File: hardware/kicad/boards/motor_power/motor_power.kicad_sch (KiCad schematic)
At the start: 65 parts, among them J1 PWM fra MCU, J2 MCP PWM, J3 DC Motor, J4 3-fase ind, J5 3-fase ud, J6 V1 ud til load, Q1 IRF540N, Q2 IRF530, SW1 Switch, U1 MCP601, U10 IL300, U11 MCP601, U2 NE555, U3 ILD74, U4 MCP601, U5 IR2110, U6 LM7805, U7 4N25, U8 IR2110, U9 MCP601

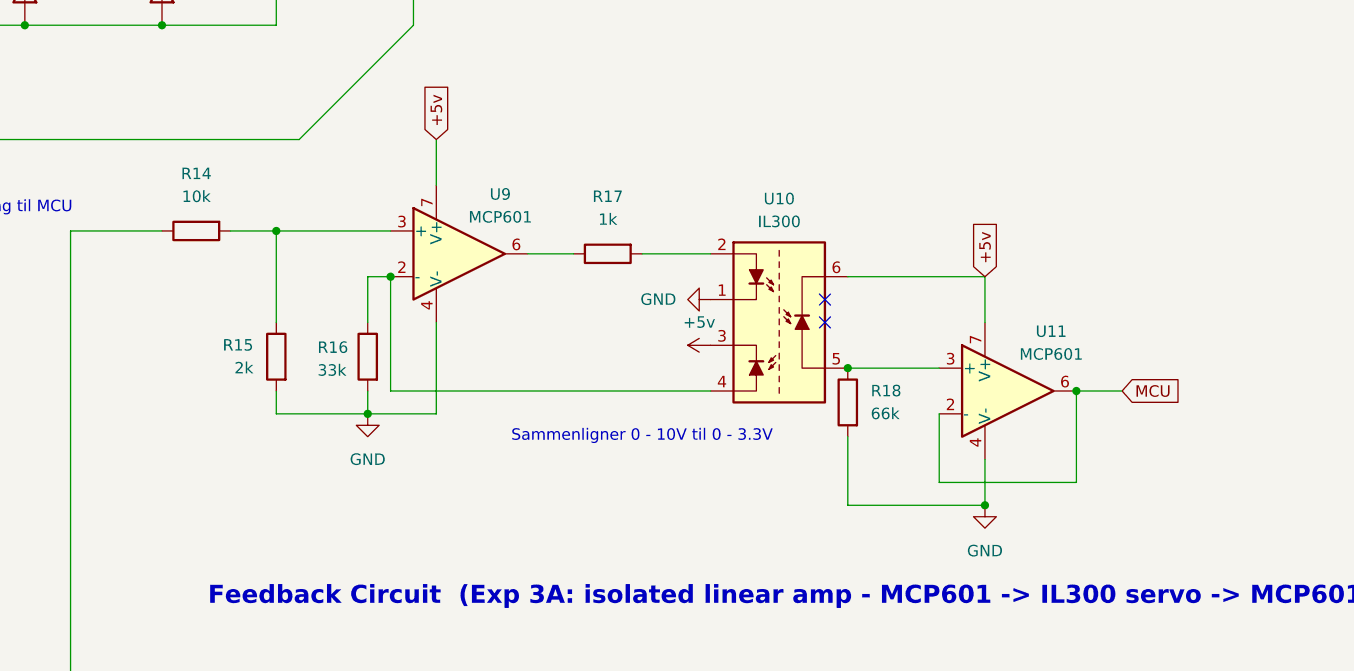
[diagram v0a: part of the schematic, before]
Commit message: motor_power: remove feedback amp and its leftover wiring (ERC 0, 57 parts)
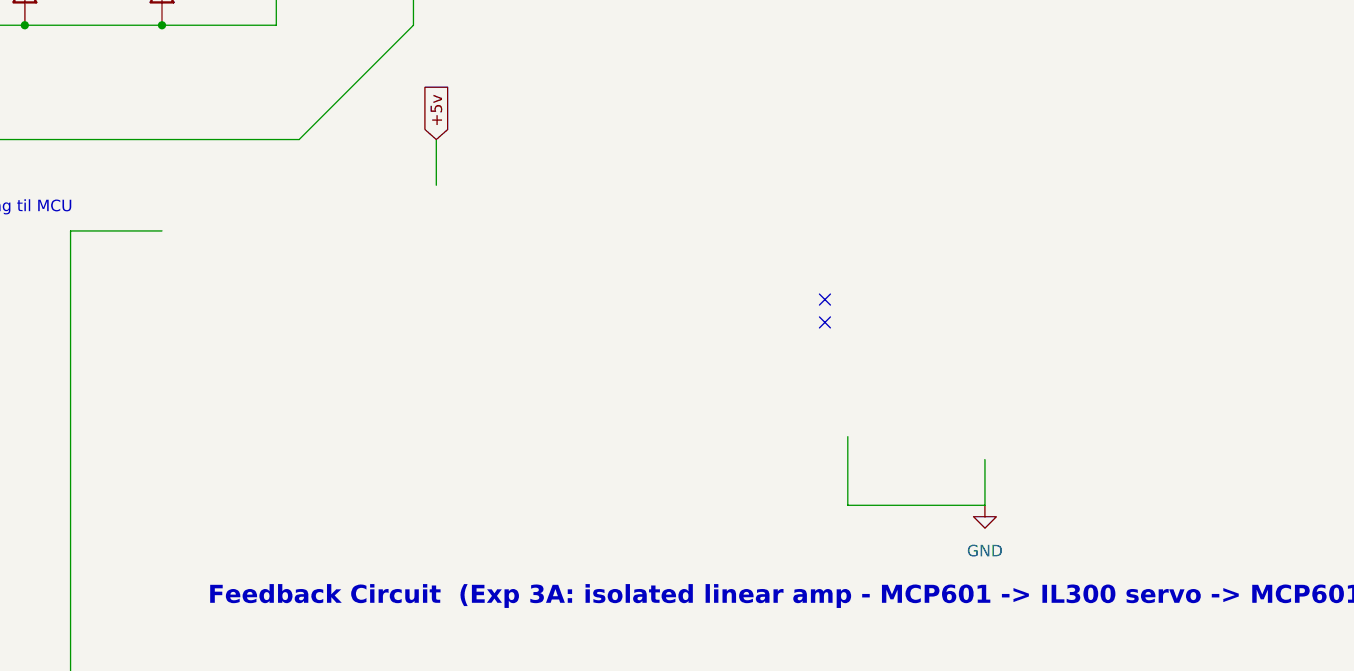
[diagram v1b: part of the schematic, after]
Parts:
- removed R14: 10k, Resistor_THT:R_Axial_DIN0207_L6.3mm_D2.5mm_P7.62mm_Horizontal, symbol Device:R
- removed R15: 2k, Resistor_THT:R_Axial_DIN0207_L6.3mm_D2.5mm_P7.62mm_Horizontal, symbol Device:R
- removed R16: 33k, Resistor_THT:R_Axial_DIN0207_L6.3mm_D2.5mm_P7.62mm_Horizontal, symbol Device:R
- removed R17: 1k, Resistor_THT:R_Axial_DIN0207_L6.3mm_D2.5mm_P7.62mm_Horizontal, symbol Device:R
- removed R18: 66k, Resistor_THT:R_Axial_DIN0207_L6.3mm_D2.5mm_P7.62mm_Horizontal, symbol Device:R
- removed U10: IL300, Package_DIP:DIP-8_W7.62mm_LongPads, symbol Isolator_Analog:IL300
- removed U11, U9: MCP601, Package_DIP:DIP-8_W7.62mm_LongPads, symbol Amplifier_Operational:MCP601-xP
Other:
- note removed: "Sammenligner 0 - 10V til 0 - 3.3V"

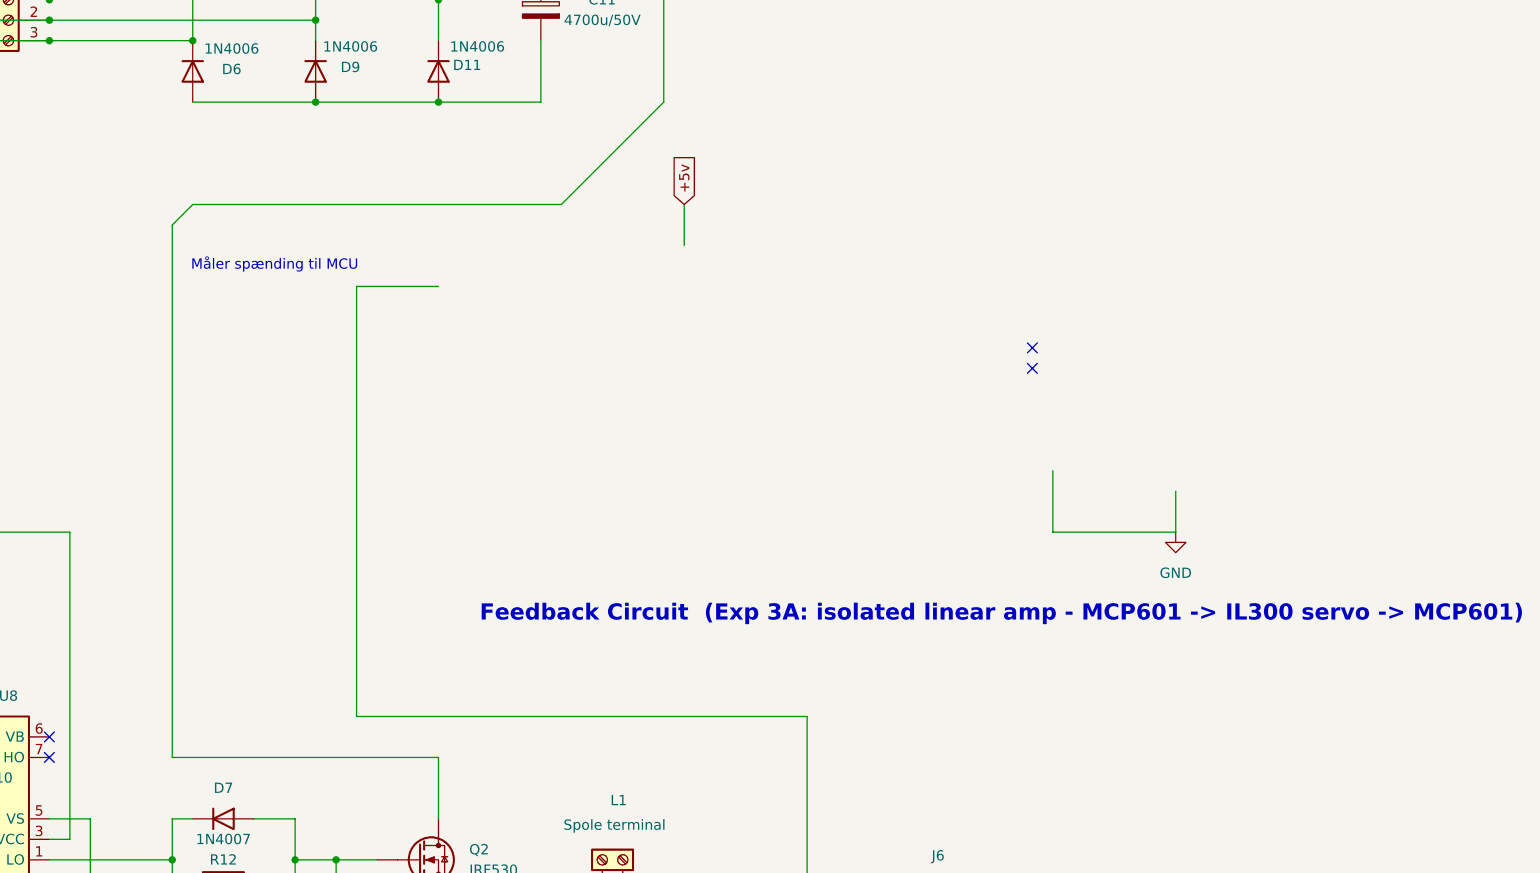
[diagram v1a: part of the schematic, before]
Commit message: motor_power: add J7 V1/GND/+5v sense connector to the feedback board
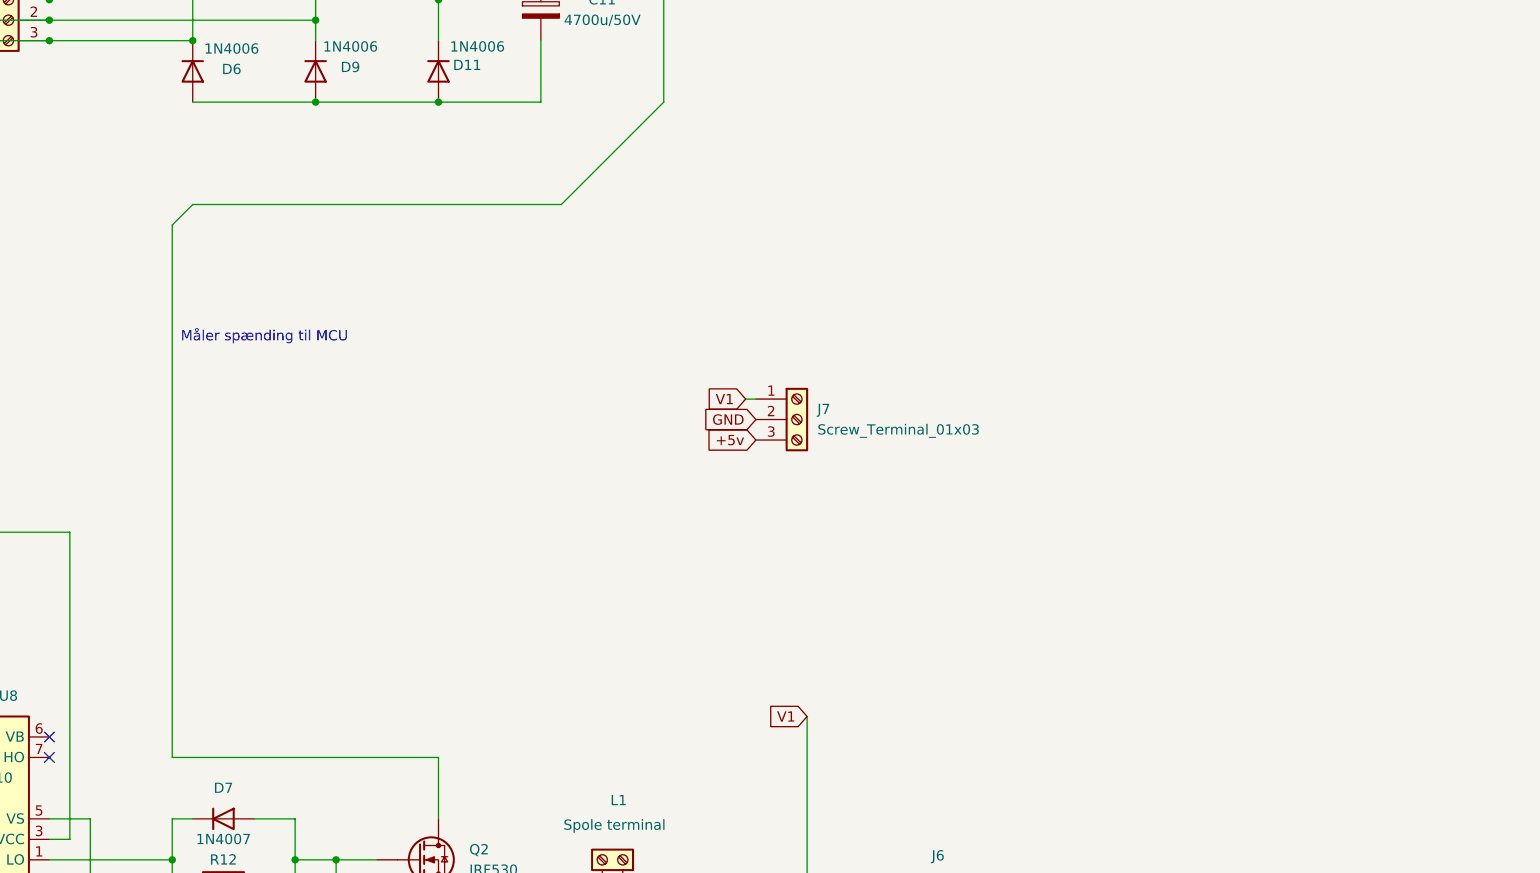
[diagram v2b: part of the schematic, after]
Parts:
- added J7: Screw_Terminal_01x03, TerminalBlock:TerminalBlock_bornier-3_P5.08mm, symbol Connector:Screw_Terminal_01x03
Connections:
- net +5v: now also J7.3 (Pin_3)
- net GND: now also J7.2 (Pin_2)
- net V1: now reaches C12.2 (Pin_2), J6.2 (Pin_2), L1.1 (Pin_1)
- net V1: now also J7.1 (Pin_1)
- no-connect marks 7 -> 5
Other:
- note removed: "Feedback Circuit (Exp 3A: isolated linear amp - MCP601 -> IL300 servo -> MCP601)"

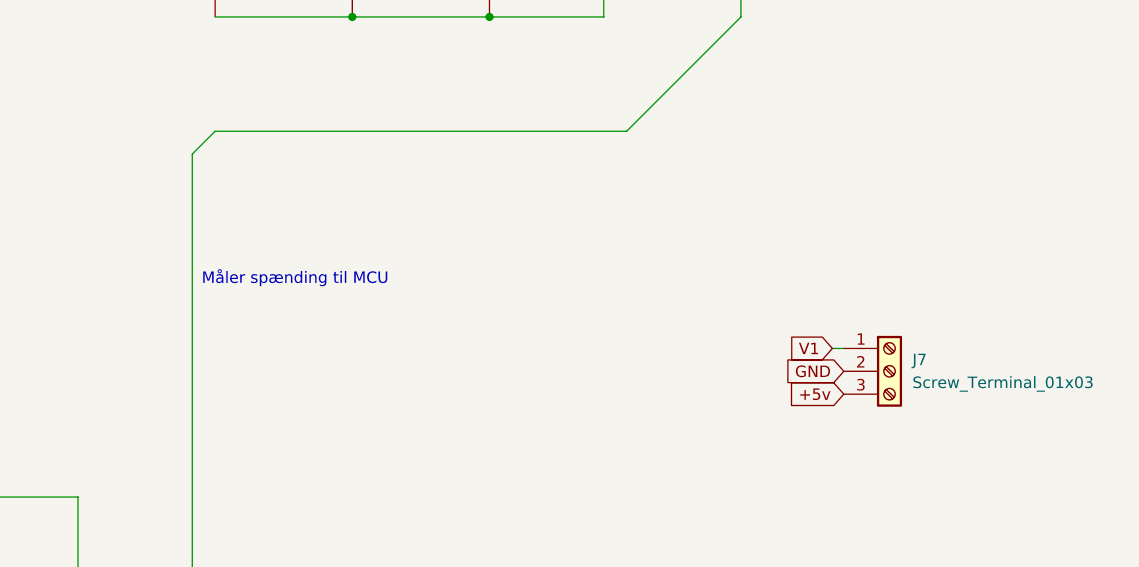
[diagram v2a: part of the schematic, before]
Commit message: Assign G/D/S TO-220 footprint to Q_NMOS MOSFETs across boards (match symbol pins)
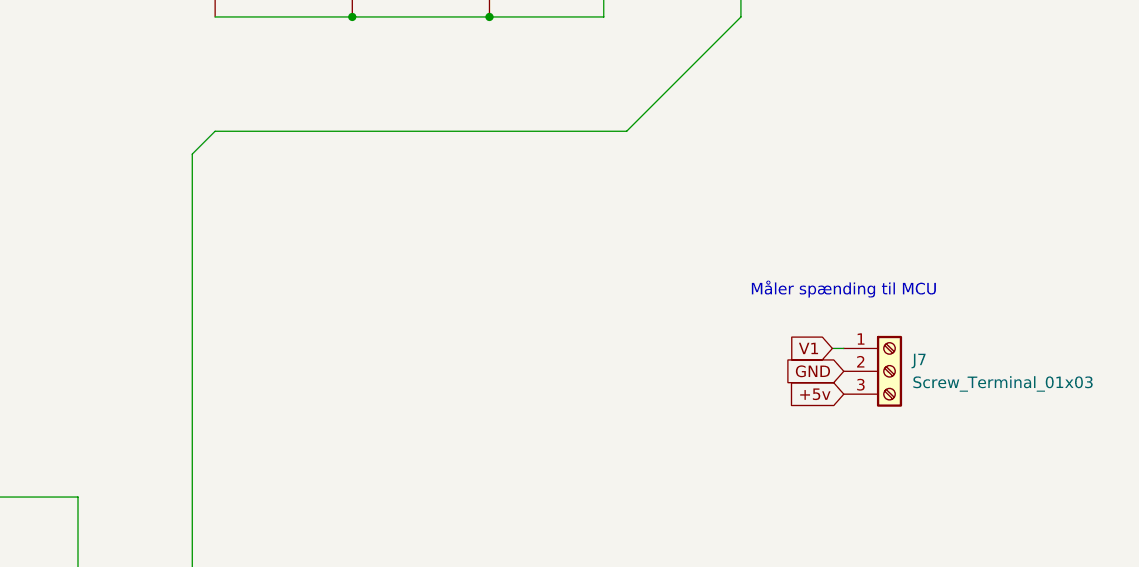
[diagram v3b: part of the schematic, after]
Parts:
- Q2: footprint energy_system:TO-220-3_Vertical_LaserPads -> energy_system:TO-220-3_Vertical_LaserPads_GDS
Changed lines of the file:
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@@
 	(text "Måler spænding til MCU\n"
 		(exclude_from_sim no)
-		(at 245.11 146.05 0)
+		(at 306.07 147.32 0)
 		(effects
 			(font
@@
 			)
 		)
-		(property "Footprint" "energy_system:TO-220-3_Vertical_LaserPads"
+		(property "Footprint" "energy_system:TO-220-3_Vertical_LaserPads_GDS"
 			(at 269.24 208.28 0)
 			(hide yes)

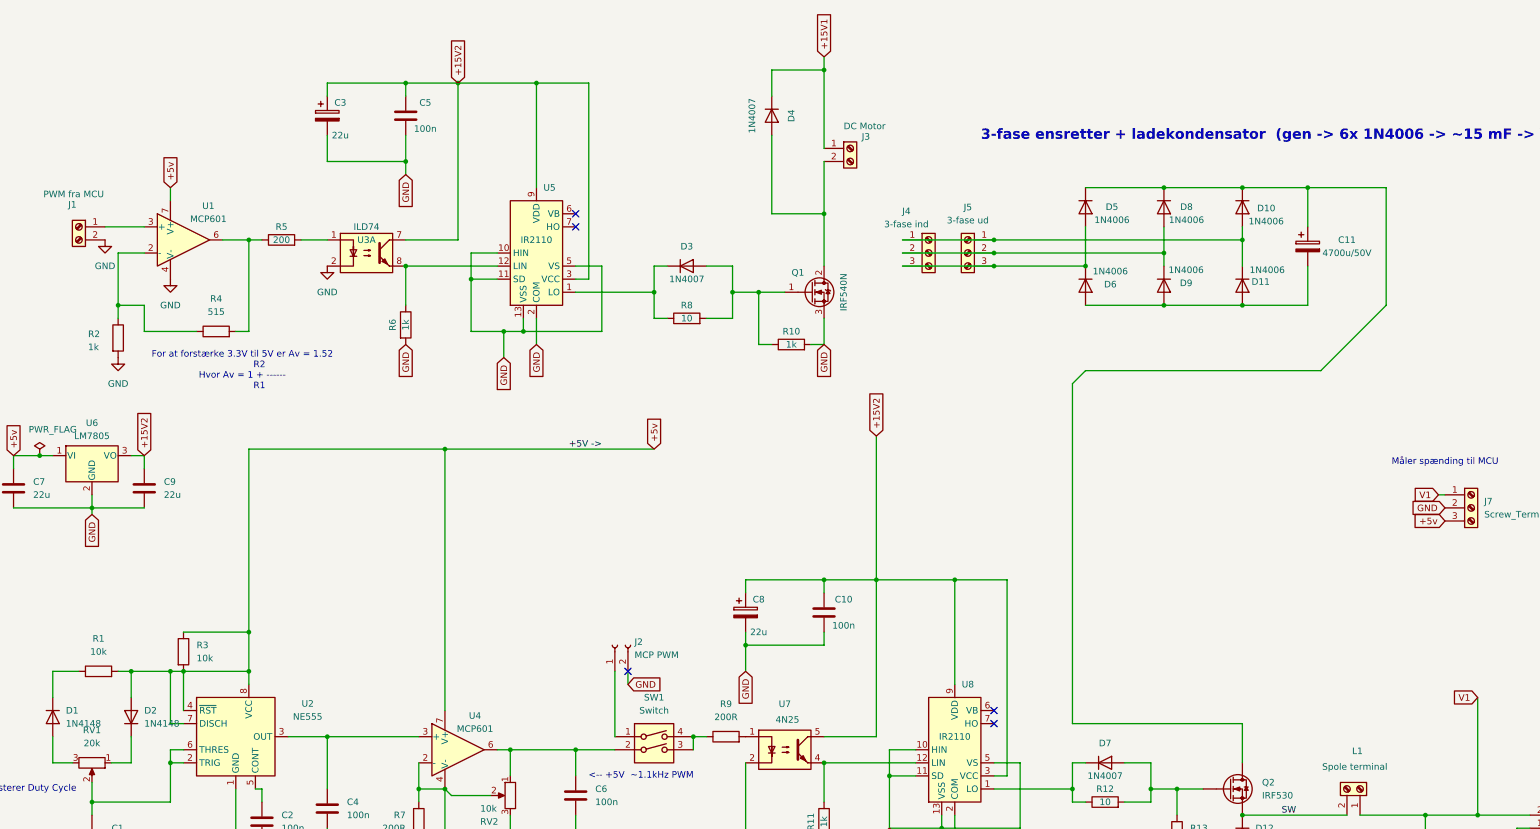
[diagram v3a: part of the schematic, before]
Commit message: system PCB: lock double-sided CNC integration (Phase 0-2.2)
Set up the whole-system board as one double-sided CNC-milled PCB.

- system.kicad_pro: CNC double-sided netclass (clearance 1.0 mm, track 1.0 mm,
  hand-stitch via 2.4/1.0 mm) replacing the laser 0.8 mm rules
- interface contract (docs/superpowers/specs/2026-06-27-...) + rewritten
  label howto for the 5-board split-MCU integration
- split MCU: Arduino owns MPPT (PV INA219 + drives mppt_buck PWM at 5 V),
  C2000 runs motor-buck + boost PID; the two MCUs are fully independent
- current_sense (discrete) dropped; current sensing via PV INA219
- c2000_feedback: strip I-channels + PWM pass, keep 3 V-dividers
  (V1/LOAD/STORE -> ADC)
- hierarchical labels placed on the 5 boards (motor_power, motor_feedback,
  mppt_buck, boost_v2_mill, c2000_feedback) for the system top sheet
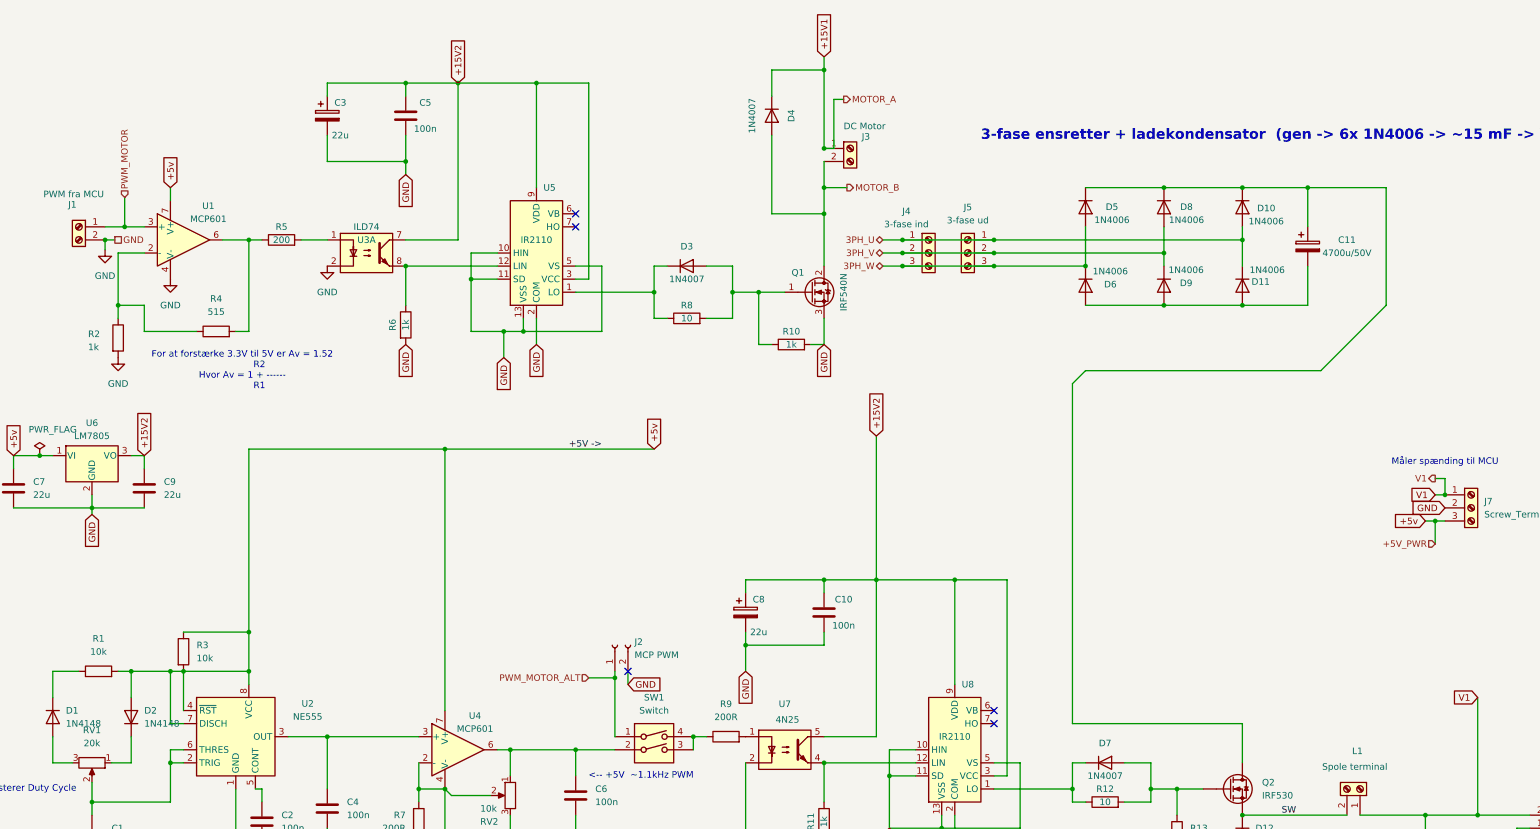
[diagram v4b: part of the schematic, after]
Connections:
- net 3PH_W: now reaches D5.2 (A), D6.1 (K), J4.3 (Pin_3), J5.3 (Pin_3)
- net 3PH_U: now reaches D10.2 (A), D11.1 (K), J4.1 (Pin_1), J5.1 (Pin_1)
- net MOTOR_B: now reaches D4.2 (A), J3.2 (Pin_2), Q1.2 (D)
- net 3PH_V: now reaches D8.2 (A), D9.1 (K), J4.2 (Pin_2), J5.2 (Pin_2)
- net PWM_MOTOR_ALT: now reaches J2.1 (Pin_1), SW1.1
- net PWM_MOTOR: now reaches J1.1 (Pin_1), U1.3 (+)
